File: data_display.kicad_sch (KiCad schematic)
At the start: 17 parts, among them IC1 ATF16V8B

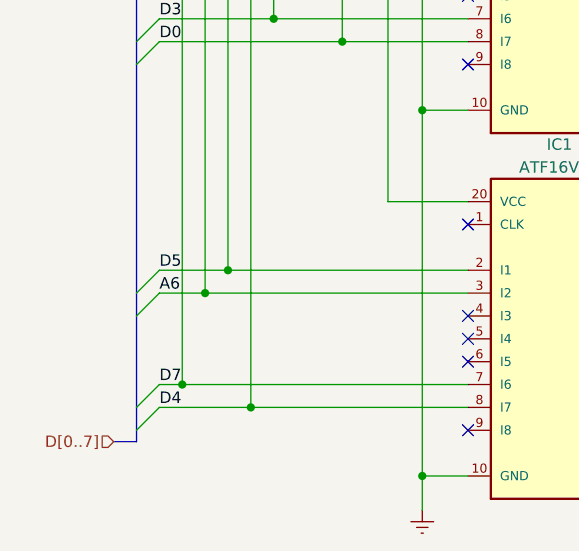
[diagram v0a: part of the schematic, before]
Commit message: RS-232/ACIA works!
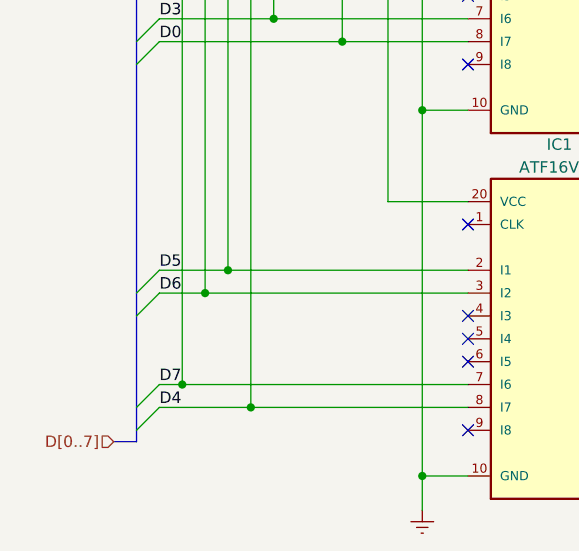
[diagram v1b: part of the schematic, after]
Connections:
- net A6 renamed D6
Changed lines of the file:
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@@
     (effects (font (size 1.27 1.27)) (justify left bottom))
   )
-  (label "A6" (at 25.4 83.82 0) (fields_autoplaced)
+  (label "D6" (at 25.4 83.82 0) (fields_autoplaced)
     (effects (font (size 1.27 1.27)) (justify left bottom))
   )
